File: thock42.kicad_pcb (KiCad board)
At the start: 2 copper layers, 132 x 104.7 mm, 78 parts, among them J1 OLED-128x32, SW1 SW_Push, SW10 SW_Push, SW11 SW_Push, SW12 SW_Push, SW13 SW_Push, SW14 SW_Push, SW15 SW_Push, SW16 SW_Push, SW17 SW_Push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

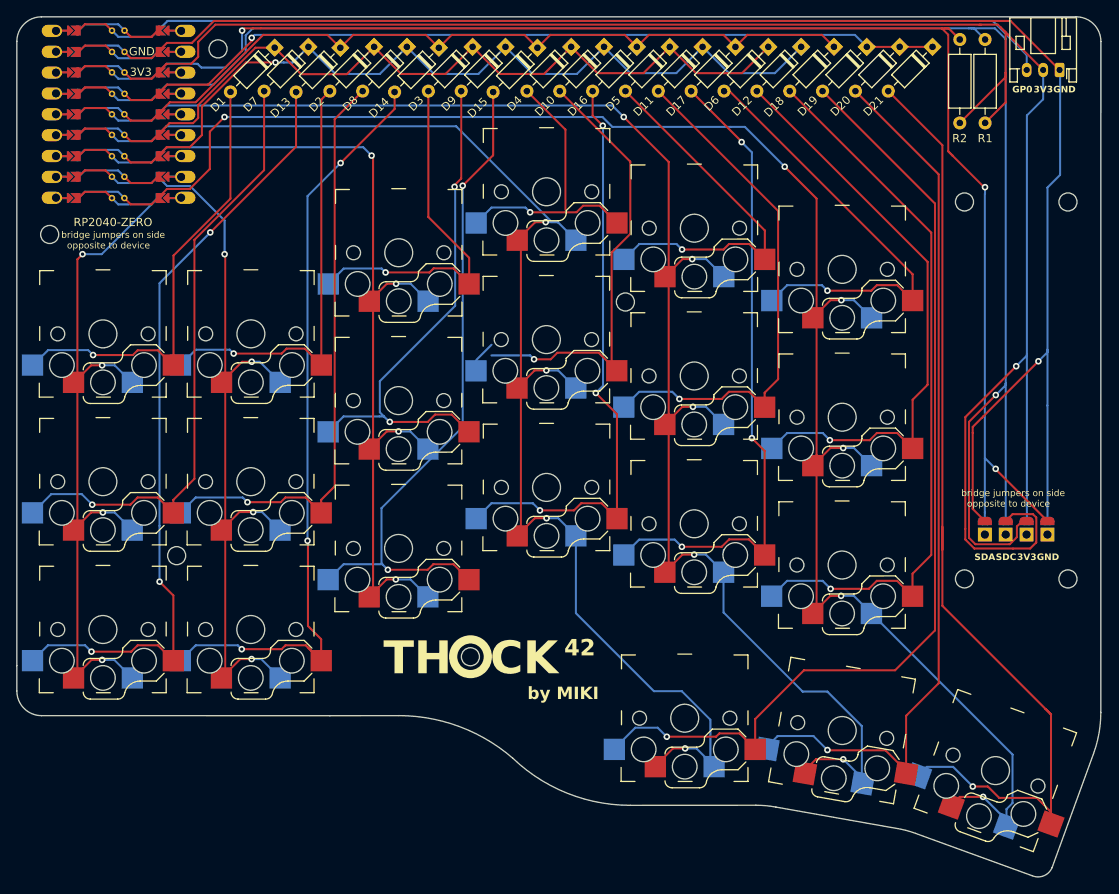
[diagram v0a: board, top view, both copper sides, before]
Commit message: fix clearance errors
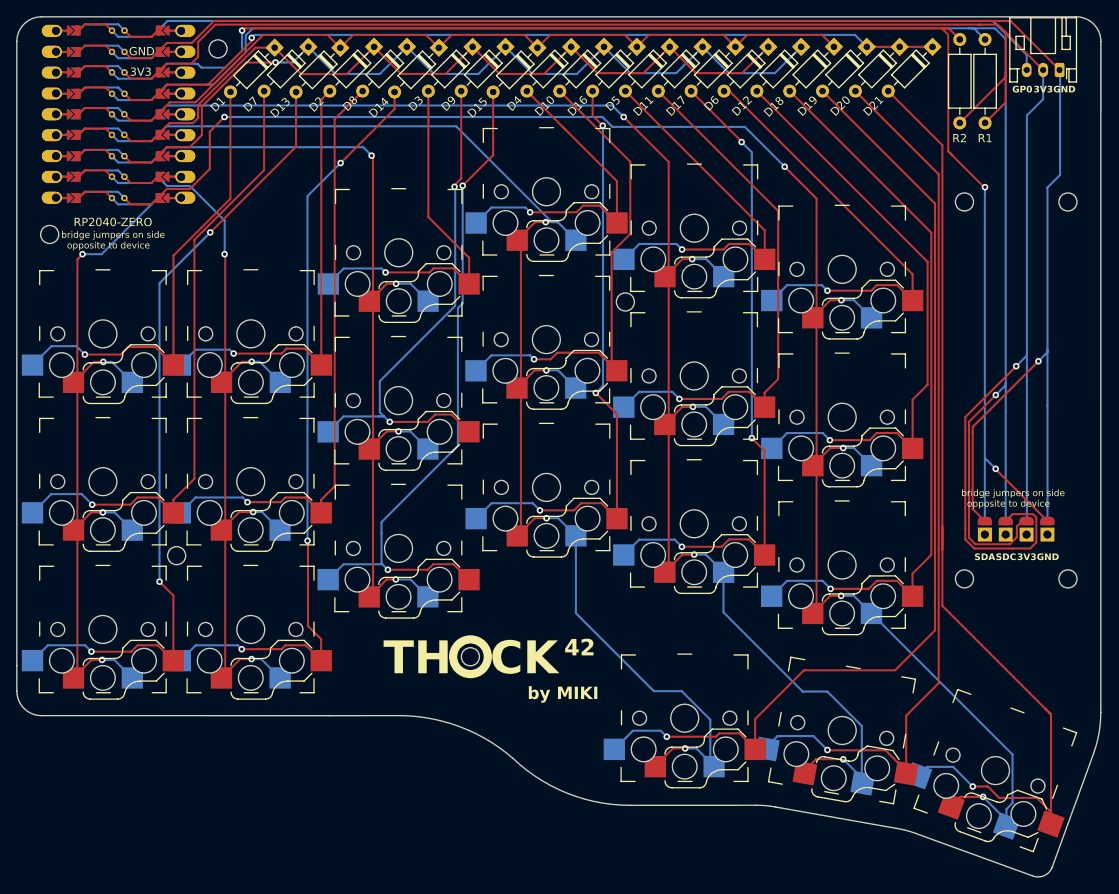
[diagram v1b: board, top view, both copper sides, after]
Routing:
- net Net-(D4-A): track 35.8 -> 40.4 mm
- net Net-(D14-A): track 95.7 -> 93.4 mm
- net COL4: track 188.3 -> 187.6 mm
- net Net-(D1-A): track 55.9 -> 56.6 mm
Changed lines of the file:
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@@
 	)
 	(segment
+		(start 98.66 89.12)
+		(end 99.57 88.21)
+		(width 0.25)
+		(layer "F.Cu")
+		(net 1)
+	)
+	(segment
 		(start 105.075 89.8)
 		(end 105.075 89.2)
@@
 	)
 	(segment
-		(start 95.285 89.18)
-		(end 100.13335 89.18)
+		(start 99.57 88.21)
+		(end 102.865 88.21)
 		(width 0.25)
 		(layer "F.Cu")
@@
 	)
 	(segment
-		(start 100.70835 88.605)
-		(end 103.185 88.605)
+		(start 94.29 89.12)
+		(end 98.66 89.12)
 		(width 0.25)
 		(layer "F.Cu")
@@
 	)
 	(segment
-		(start 103.185 88.605)
-		(end 105.06 90.48)
+		(start 102.865 88.21)
+		(end 105.06 90.405)
 		(width 0.25)
 		(layer "F.Cu")
@@
 	)
 	(segment
-		(start 100.13335 89.18)
-		(end 100.70835 88.605)
-		(width 0.25)
-		(layer "F.Cu")
-		(net 1)
-	)
-	(segment
 		(start 105.06 90.405)
 		(end 105.06 89.215)
@@
 	)
 	(via
-		(at 95.285 89.18)
+		(at 94.29 89.12)
 		(size 0.8)
 		(drill 0.4)
@@
 	)
 	(segment
-		(start 94.685 88.58)
-		(end 95.285 89.18)
+		(start 90.215 88.1)
+		(end 92.83 88.1)
+		(width 0.25)
+		(layer "B.Cu")
+		(net 1)
+	)
+	(segment
+		(start 93.27 88.1)
+		(end 94.29 89.12)
 		(width 0.25)
 		(layer "B.Cu")
@@
 	)
 	(segment
-		(start 89.81 88.58)
-		(end 94.685 88.58)
+		(start 92.83 88.1)
+		(end 93.27 88.1)
 		(width 0.25)
 		(layer "B.Cu")
@@
 	)
 	(segment
-		(start 87.91 90.48)
-		(end 89.81 88.58)
+		(start 87.91 90.405)
+		(end 90.215 88.1)
 		(width 0.25)
 		(layer "B.Cu")
@@
 	)
 	(segment
+		(start 152.8 61.734437)
+		(end 152.467782 61.402218)
+		(width 0.25)
+		(layer "F.Cu")
+		(net 4)
+	)
+	(segment
 		(start 148.5 71.8)
 		(end 152.8 71.8)
@@
 	)
 	(segment
-		(start 154.14835 71.8)
-		(end 154.94835 71)
+		(start 159.075 68.009436)
+		(end 152.467782 61.402218)
 		(width 0.25)
 		(layer "F.Cu")
@@
 	)
 	(segment
-		(start 154.94835 71)
-		(end 156.975 71)
+		(start 159.075 73.1)
+		(end 159.075 68.009436)
+		(width 0.25)
+		(layer "F.Cu")
+		(net 4)
+	)
+	(segment
+		(start 154.14835 71.8)
+		(end 154.94835 71)
 		(width 0.25)
 		(layer "F.Cu")
@@
 	)
 	(segment
-		(start 152.8 71.5)
-		(end 152.8 61.734437)
+		(start 154.94835 71)
+		(end 156.975 71)
 		(width 0.25)
 		(layer "F.Cu")
@@
 	)
 	(segment
-		(start 152.8 61.734437)
+		(start 152.467782 61.402218)
 		(end 148.110088 57.044525)
 		(width 0.25)
@@
 	)
 	(segment
-		(start 141.925 89.8)
-		(end 143.8 87.925)
+		(start 141.905 91.1)
+		(end 143.78 89.225)
 		(width 0.25)
 		(layer "B.Cu")
@@
 	)
 	(segment
-		(start 121.45 122.175)
-		(end 121.45 111.85)
+		(start 121.18415 124.525)
+		(end 118.7075 124.525)
 		(width 0.25)
 		(layer "F.Cu")
@@
 	)
 	(segment
-		(start 131.998242 59.226758)
-		(end 131.998242 57.156371)
+		(start 121.45 122.175)
+		(end 121.45 111.85)
 		(width 0.25)
 		(layer "F.Cu")
@@
 	)
 	(segment
-		(start 121.18415 124.525)
-		(end 123.05915 126.4)
+		(start 118.7075 124.525)
+		(end 118.2325 125)
 		(width 0.25)
 		(layer "F.Cu")
@@
 	)
 	(segment
-		(start 123.05915 126.4)
-		(end 121.43415 124.775)
+		(start 131.998242 59.226758)
+		(end 131.998242 57.156371)
 		(width 0.25)
 		(layer "F.Cu")
@@
 	)
 	(segment
-		(start 118.7075 124.525)
-		(end 121.18415 124.525)
+		(start 118.2325 125)
+		(end 113.38415 125)
 		(width 0.25)
 		(layer "F.Cu")
@@
 	)
 	(segment
-		(start 123.05915 123.78415)
+		(start 121.18415 124.525)
 		(end 123.05915 126.4)
 		(width 0.25)
@@
 	)
 	(segment
-		(start 113.38415 125)
-		(end 118.2325 125)
+		(start 123.05915 123.78415)
+		(end 123.05915 126.4)
 		(width 0.25)
 		(layer "F.Cu")
@@
 	)
 	(segment
-		(start 118.2325 125)
-		(end 118.7075 124.525)
-		(width 0.25)
-		(layer "F.Cu")
-		(net 14)
-	)
-	(segment
 		(start 125.425 65.8)
 		(end 131.998242 59.226758)
@@
 	)
 	(segment
-		(start 130.405 107.82)
+		(start 130.405 110.84)
 		(end 130.405 114.555)
 		(width 0.25)
@@
 	)
 	(segment
+		(start 139.71 83.491903)
+		(end 139.71 100.225)
+		(width 0.25)
+		(layer "B.Cu")
+		(net 15)
+	)
+	(segment
 		(start 130.405 114.555)
 		(end 130.505 114.655)
@@
 	)
 	(segment
-		(start 140.290623 68.563362)
-		(end 140.290623 97.934377)
+		(start 139.71 100.225)
+		(end 139.1225 100.8125)
+		(width 0.25)
+		(layer "B.Cu")
+		(net 15)
+	)
+	(segment
+		(start 139.1225 100.8125)
+		(end 130.405 109.53)
+		(width 0.25)
+		(layer "B.Cu")
+		(net 15)
+	)
+	(segment
+		(start 130.405 109.53)
+		(end 130.405 110.84)
 		(width 0.25)
 		(layer "B.Cu")
@@
 	)
 	(segment
-		(start 140.290623 97.934377)
-		(end 130.405 107.82)
+		(start 140.290623 68.563362)
+		(end 140.290623 82.91128)
+		(width 0.25)
+		(layer "B.Cu")
+		(net 15)
+	)
+	(segment
+		(start 140.290623 82.91128)
+		(end 139.71 83.491903)
 		(width 0.25)
 		(layer "B.Cu")
@@
 	)
 	(segment
-		(start 161.317542 134.554188)
-		(end 164.037543 134.554188)
+		(start 158.75 137.200001)
+		(end 161.020001 134.93)
 		(width 0.25)
 		(layer "B.Cu")
@@
 	)
 	(segment
-		(start 164.037543 134.554188)
-		(end 165.142542 135.659187)
+		(start 161.020001 134.93)
+		(end 164.413355 134.93)
 		(width 0.25)
 		(layer "B.Cu")
@@
 	)
 	(segment
-		(start 158.742542 137.129188)
-		(end 161.317542 134.554188)
+		(start 164.413355 134.93)
+		(end 165.142542 135.659187)
 		(width 0.25)
 		(layer "B.Cu")
@@
 	)
 	(segment
-		(start 172.075 112.9)
-		(end 172.075 113.555)
-		(width 0.25)
-		(layer "B.Cu")
-		(net 26)
-	)
-	(segment
 		(start 168.233325 77.5)
 		(end 169.941602 77.5)
@@
 	)
 	(segment
-		(start 92.91 92.58)
-		(end 95.057567 90.432433)
-		(width 0.25)
-		(layer "F.Cu")
-		(net 31)
-	)
-	(segment
 		(start 93.375 77.525)
 		(end 93.375 91.45)
@@
 	)
 	(segment
-		(start 95.057567 90.432433)
-		(end 96.382735 90.432433)
-		(width 0.25)
-		(layer "F.Cu")
-		(net 31)
-	)
-	(segment
 		(start 92.925 91.9)
 		(end 93.375 92.35)
@@
 	)
 	(segment
+		(start 92.91 92.505)
+		(end 95.395 90.02)
+		(width 0.25)
+		(layer "F.Cu")
+		(net 31)
+	)
+	(segment
 		(start 95.10915 126.3)
 		(end 96.38415 126.3)
@@
 	)
 	(segment
+		(start 95.395 90.02)
+		(end 96.53 90.02)
+		(width 0.25)
+		(layer "F.Cu")
+		(net 31)
+	)
+	(segment
 		(start 93.375 91.45)
 		(end 92.925 91.9)
@@
 	)
 	(via
-		(at 96.382735 90.432433)
+		(at 94 76.9)
 		(size 0.8)
 		(drill 0.4)
@@
 	)
 	(via
-		(at 94 76.9)
+		(at 96.48 108.35)
 		(size 0.8)
 		(drill 0.4)
@@
 	)
 	(via
-		(at 96.48 108.35)
+		(at 96.38415 126.3)
 		(size 0.8)
 		(drill 0.4)
@@
 	)
 	(via
-		(at 96.38415 126.3)
+		(at 96.53 90.02)
 		(size 0.8)
 		(drill 0.4)
@@
 	)
 	(segment
-		(start 97.912433 90.432433)
-		(end 100.06 92.58)
+		(start 97.575 90.02)
+		(end 100.06 92.505)
 		(width 0.25)
 		(layer "B.Cu")
@@
 	)
 	(segment
-		(start 96.382735 90.432433)
-		(end 97.912433 90.432433)
+		(start 96.53 90.02)
+		(end 97.575 90.02)
 		(width 0.25)
 		(layer "B.Cu")

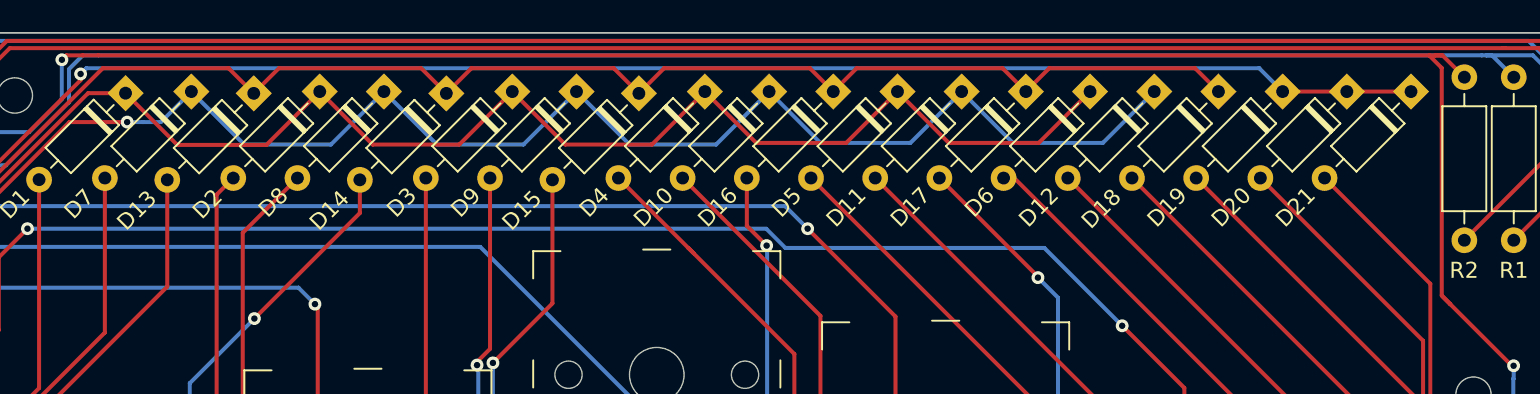
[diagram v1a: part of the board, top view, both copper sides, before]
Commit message: add silkscreen for resistors on backside
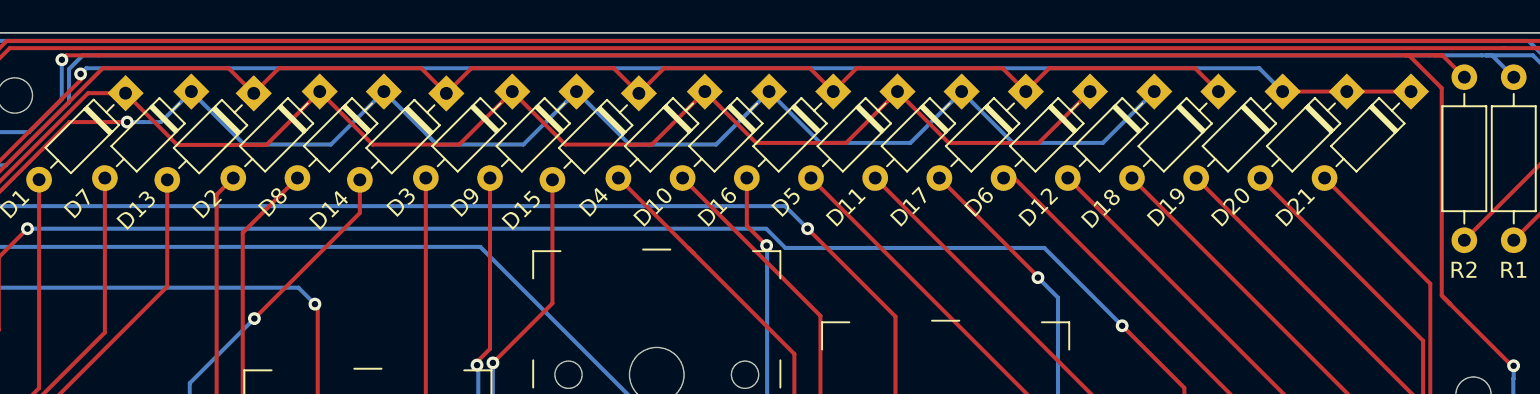
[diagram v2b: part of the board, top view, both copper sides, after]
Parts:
- added ?: , clipboard:91b5afe0-6e02-4eea-9984-07a5be6dfd2b, B.Cu at (202.2, 59.1)
- added ?: , clipboard:91b5afe0-6e02-4eea-9984-07a5be6dfd2b, B.Cu at (205.3, 59.1)
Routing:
- net OLED_SDA: track 176.3 -> 177.0 mm
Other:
- board text added: "R1"
- board text added: "R2"

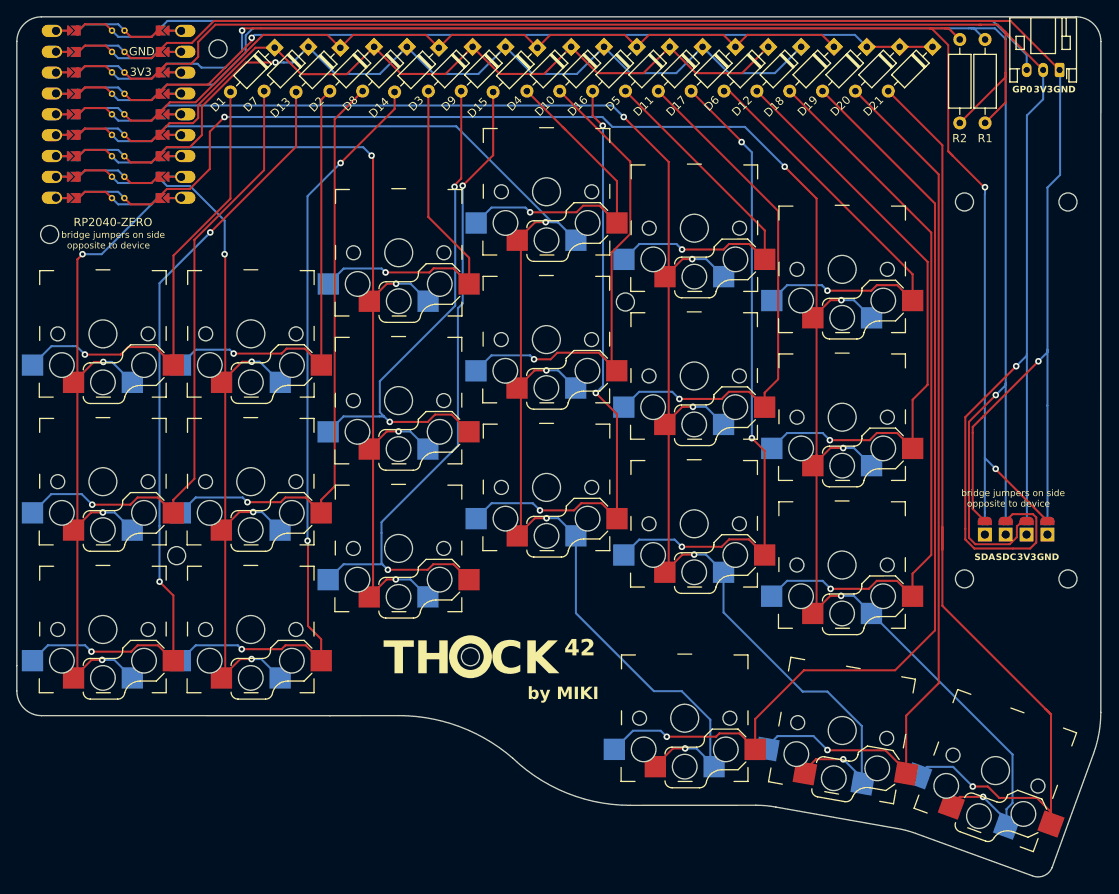
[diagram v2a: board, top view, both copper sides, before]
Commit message: move index col down to match ring col and fix tolerance error
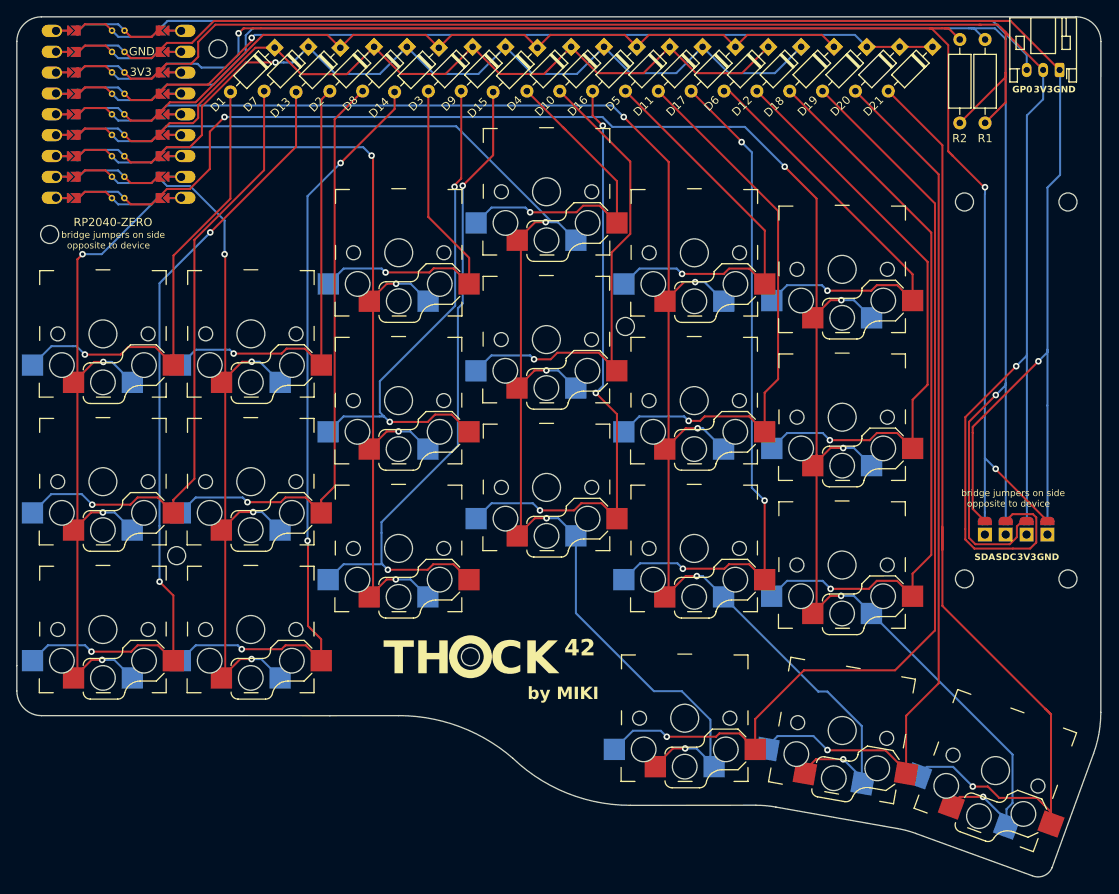
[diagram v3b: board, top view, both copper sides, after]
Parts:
- moved SW11 3.00 mm to (168.5, 94.7)
- moved SW17 3.00 mm to (168.5, 112.7)
- moved SW5 3.00 mm to (168.5, 76.7)
- moved REF** 2.98 mm to (160.1, 85.7)
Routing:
- net Net-(D5-A): track 46.0 -> 49.8 mm
- net Net-(D17-A): track 79.6 -> 82.4 mm
- net Net-(D11-A): track 64.6 -> 67.4 mm
- net COL4: track 187.6 -> 186.2 mm
